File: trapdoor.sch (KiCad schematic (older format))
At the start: 2 parts, among them P9 TRAPDOOR

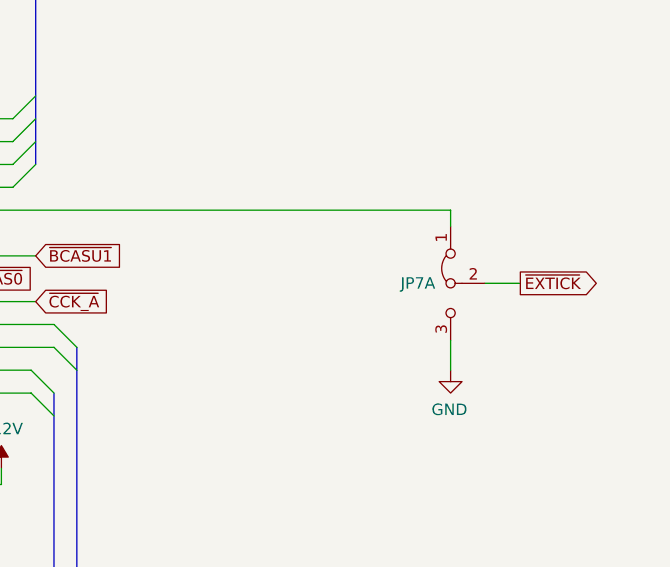
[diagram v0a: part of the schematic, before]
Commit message: Replace RAM with original design
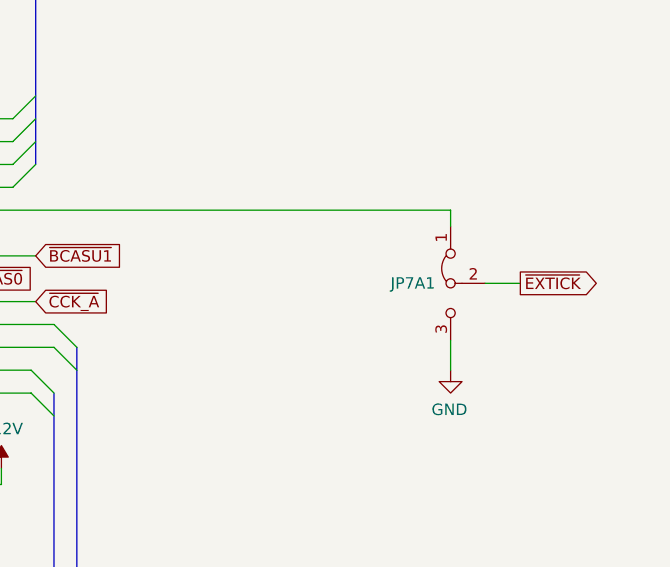
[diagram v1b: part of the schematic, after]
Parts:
- JP7A1: renamed from JP7A; footprint Raemixx500:Jumper3-Bridged12 -> Raemixx500:Jumper3-Open
- P9: footprint MODULE -> Connector_PinHeader_2.54mm:PinHeader_2x28_P2.54mm_Horizontal
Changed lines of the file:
@@
 F 0 "P9" H 6155 5445 50  0000 C CNN
 F 1 "TRAPDOOR" H 6155 5354 50  0000 C CNN
-F 2 "MODULE" H 6155 3730 50  0001 C CNN
+F 2 "Connector_PinHeader_2.54mm:PinHeader_2x28_P2.54mm_Horizontal" H 6155 3730 50  0001 C CNN
 F 3 "DOCUMENTATION" H 6155 3730 50  0001 C CNN
 	1    6155 3730
@@
 AR Path="/5D2DC3A1/5D01CBE0" Ref="#PWR?"  Part="1"
 AR Path="/5E813DC5/5D01CBE0" Ref="#PWR?"  Part="1"
-AR Path="/5D00C589/5D01CBE0" Ref="#PWR?"  Part="1"
-F 0 "#PWR?" H 7740 5110 50  0001 C CNN
+AR Path="/5D00C589/5D01CBE0" Ref="#PWR0252"  Part="1"
+F 0 "#PWR0252" H 7740 5110 50  0001 C CNN
 F 1 "-12V" H 7755 5183 50  0000 C CNN
 F 2 "" H 7740 5010 50  0001 C CNN
@@
 P 4590 5010
 AR Path="/5E813DC5/5D01CBE6" Ref="#PWR?"  Part="1"
-AR Path="/5D00C589/5D01CBE6" Ref="#PWR?"  Part="1"
-F 0 "#PWR?" H 4590 4860 50  0001 C CNN
+AR Path="/5D00C589/5D01CBE6" Ref="#PWR0253"  Part="1"
+F 0 "#PWR0253" H 4590 4860 50  0001 C CNN
 F 1 "+12V" H 4605 5183 50  0000 C CNN
 F 2 "" H 4590 5010 50  0001 C CNN
@@
 	5200 2480 5200 3380
 $Comp
-L power:GND #PWR?
+L power:GND #PWR0254
 U 1 1 5D01F772
 P 5200 5725
-F 0 "#PWR?" H 5200 5475 50  0001 C CNN
+F 0 "#PWR0254" H 5200 5475 50  0001 C CNN
 F 1 "GND" H 5205 5552 50  0000 C CNN
 F 2 "" H 5200 5725 50  0001 C CNN
@@
 	5200 4980 5200 5725
 $Comp
-L power:GND #PWR?
+L power:GND #PWR0255
 U 1 1 5D021162
 P 7110 5725
-F 0 "#PWR?" H 7110 5475 50  0001 C CNN
+F 0 "#PWR0255" H 7110 5475 50  0001 C CNN
 F 1 "GND" H 7115 5552 50  0000 C CNN
 F 2 "" H 7110 5725 50  0001 C CNN
@@
 	7225 4880 7225 2380
 $Comp
-L power:VCC #PWR?
+L power:VCC #PWR0256
 U 1 1 5D0263FC
 P 7225 1660
-F 0 "#PWR?" H 7225 1510 50  0001 C CNN
+F 0 "#PWR0256" H 7225 1510 50  0001 C CNN
 F 1 "VCC" H 7242 1833 50  0000 C CNN
 F 2 "" H 7225 1660 50  0001 C CNN
@@
 P 9705 4200
 AR Path="/5E7E9EC4/5D0BD392" Ref="JP7B?"  Part="1"
-AR Path="/5D00C589/5D0BD392" Ref="JP7A"  Part="1"
-F 0 "JP7A" V 9705 4267 50  0000 L CNN
+AR Path="/5D00C589/5D0BD392" Ref="JP7A1"  Part="1"
+F 0 "JP7A1" V 9705 4267 50  0000 L CNN
 F 1 "Jumper_3_Bridged12" V 9660 4266 50  0001 L CNN
-F 2 "Raemixx500:Jumper3-Bridged12" H 9705 4200 50  0001 C CNN
+F 2 "Raemixx500:Jumper3-Open" H 9705 4200 50  0001 C CNN
 F 3 "~" H 9705 4200 50  0001 C CNN
 	1    9705 4200
@@
 	6905 3880 9705 3880
 $Comp
-L power:GND #PWR?
+L power:GND #PWR0257
 U 1 1 5D0CF224
 P 9705 4580
-F 0 "#PWR?" H 9705 4330 50  0001 C CNN
+F 0 "#PWR0257" H 9705 4330 50  0001 C CNN
 F 1 "GND" H 9710 4407 50  0000 C CNN
 F 2 "" H 9705 4580 50  0001 C CNN

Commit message: Use proper trapdoor footprint at last
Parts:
- P9: footprint Connector_PinHeader_2.54mm:PinHeader_2x28_P2.54mm_Horizontal -> Raemixx500:Trapdoor
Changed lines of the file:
@@
 F 0 "P9" H 6155 5445 50  0000 C CNN
 F 1 "TRAPDOOR" H 6155 5354 50  0000 C CNN
-F 2 "Connector_PinHeader_2.54mm:PinHeader_2x28_P2.54mm_Horizontal" H 6155 3730 50  0001 C CNN
+F 2 "Raemixx500:Trapdoor" H 6155 3730 50  0001 C CNN
 F 3 "DOCUMENTATION" H 6155 3730 50  0001 C CNN
 	1    6155 3730

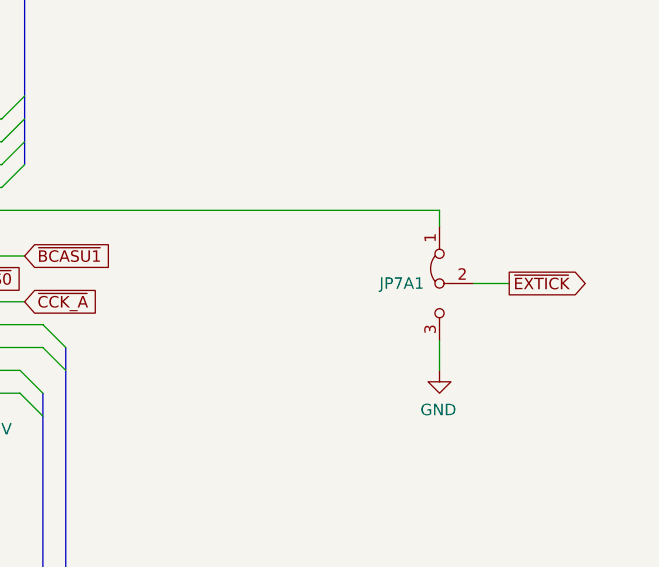
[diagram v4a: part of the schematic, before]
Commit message: Fix JP7A/B
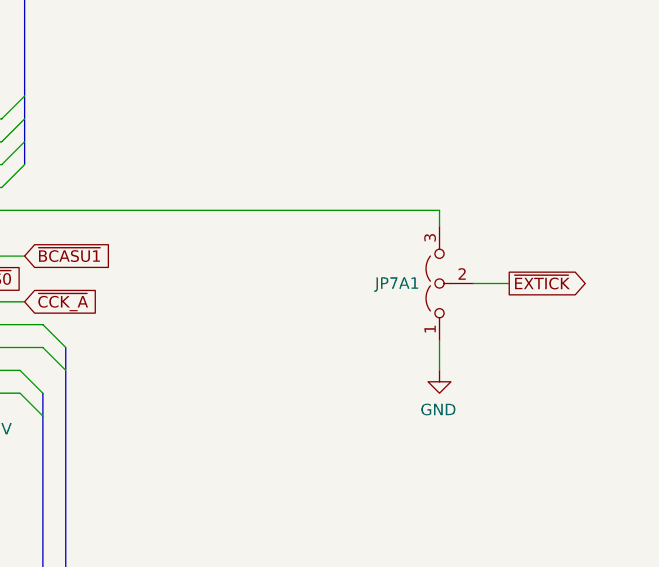
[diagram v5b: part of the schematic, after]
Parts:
- removed JP7A1: Jumper_3_Bridged12, Raemixx500:Jumper3-Open, symbol Jumper:Jumper_3_Bridged12
- added JP7A1: Jumper_3_Open, Raemixx500:Jumper3-Open, symbol Jumper_3_Bridged23:Jumper_3_Open
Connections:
- net GND: now also JP7A1.1 (A)
- net ~EXTICK: now also JP7A1.2 (C)
- net at P9.32 (PIN32): now also JP7A1.3 (B)
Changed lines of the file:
@@
 encoding utf-8
 Sheet 14 14
-Title ""
-Date ""
-Rev ""
-Comp ""
+Title "Rämixx500"
+Date "2020-04-05"
+Rev "1git"
+Comp "SukkoPera"
 Comment1 ""
 Comment2 ""
 Comment3 ""
-Comment4 ""
+Comment4 "Licensed under CERN OHL v.1.2"
 $EndDescr
 $Comp
@@
 	7890 1360 4420 1360
 Connection ~ 4420 1360
-$Comp
-L Jumper:Jumper_3_Bridged12 JP7B?
-U 1 1 5D0BD392
-P 9705 4200
-AR Path="/5E7E9EC4/5D0BD392" Ref="JP7B?"  Part="1"
-AR Path="/5D00C589/5D0BD392" Ref="JP7A1"  Part="1"
-F 0 "JP7A1" V 9705 4267 50  0000 L CNN
-F 1 "Jumper_3_Bridged12" V 9660 4266 50  0001 L CNN
-F 2 "Raemixx500:Jumper3-Open" H 9705 4200 50  0001 C CNN
-F 3 "~" H 9705 4200 50  0001 C CNN
-	1    9705 4200
-	0    -1   1    0
-$EndComp
 Wire Wire Line
 	9705 4450 9705 4580
@@
 Text GLabel 5065 3980 0    50   Input ~ 0
 ~CLKCS
+$Comp
+L Jumper_3_Bridged23:Jumper_3_Open JP7A1
+U 1 1 5E92560D
+P 9705 4200
+F 0 "JP7A1" V 9705 4287 50  0000 L CNN
+F 1 "Jumper_3_Open" V 9660 4287 50  0001 L CNN
+F 2 "Raemixx500:Jumper3-Open" H 9705 4200 50  0001 C CNN
+F 3 "~" H 9705 4200 50  0001 C CNN
+	1    9705 4200
+	0    -1   -1   0
+$EndComp
 Wire Bus Line
 	7970 4680 7970 5480
